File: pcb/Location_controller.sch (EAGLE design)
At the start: 62 parts, among them IC1 LIS302DL

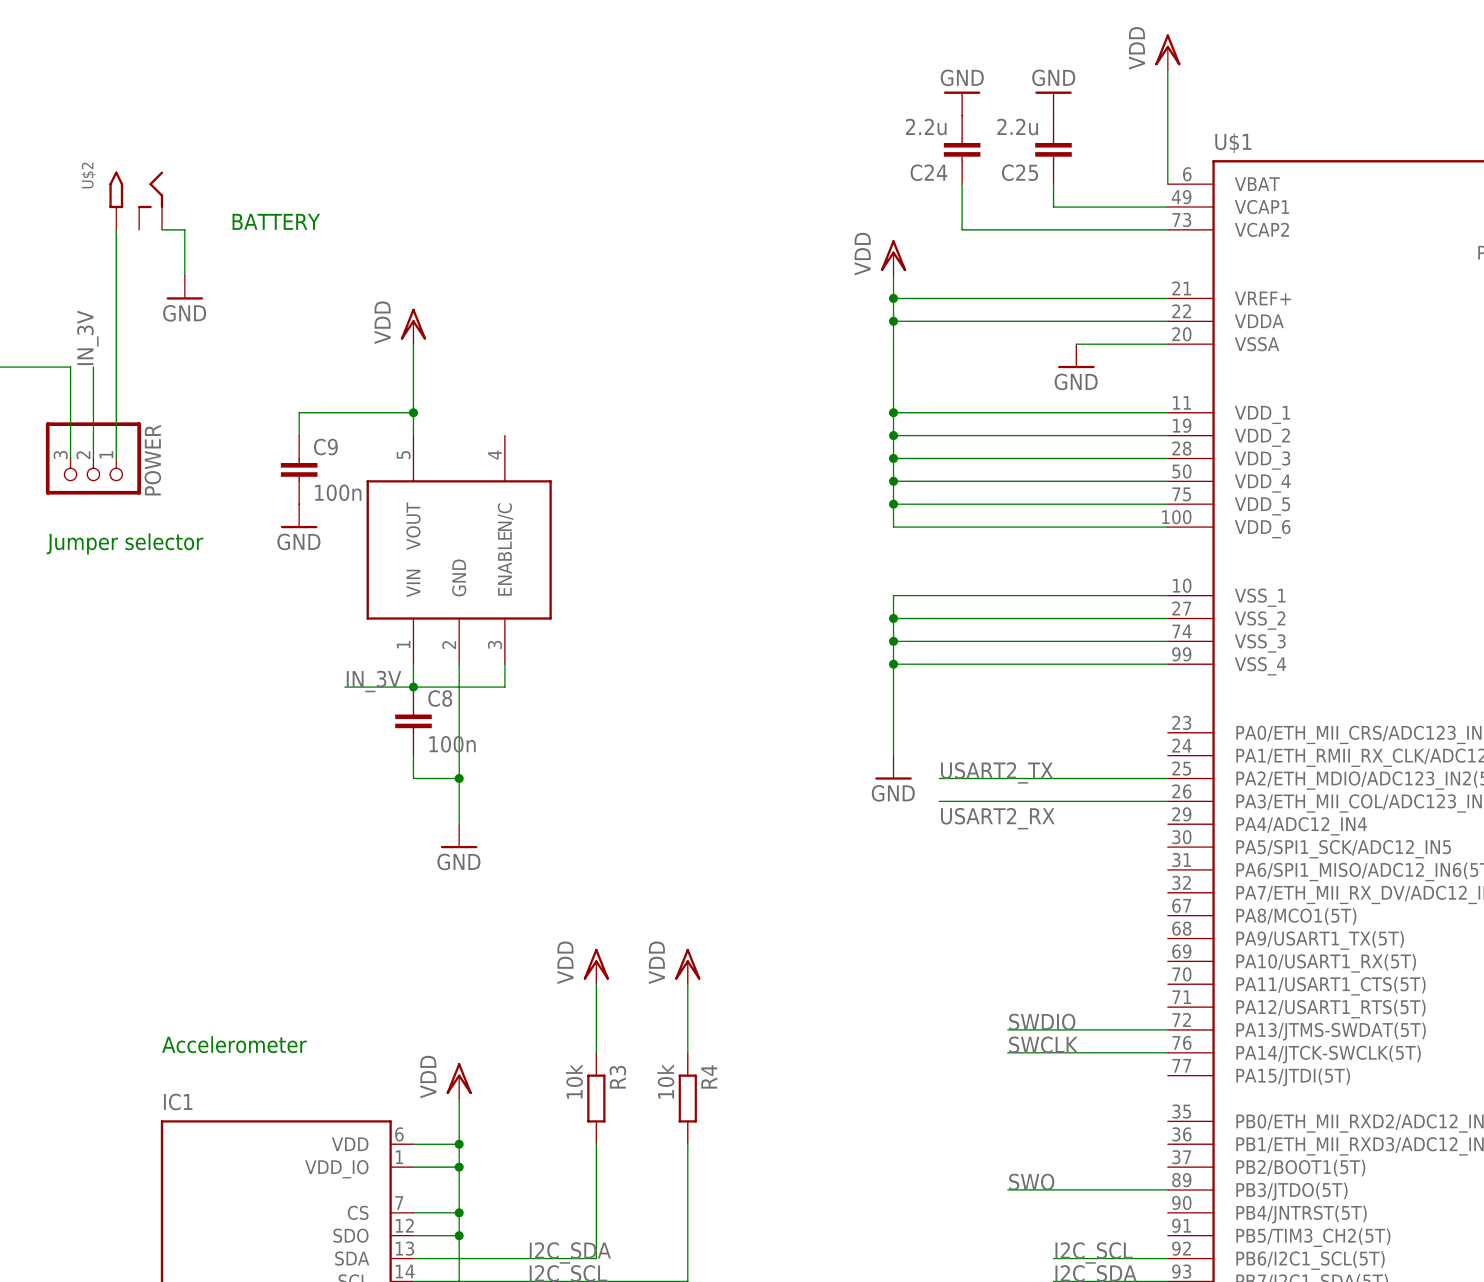
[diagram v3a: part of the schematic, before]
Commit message: Move RCM_POWER pins to correct position
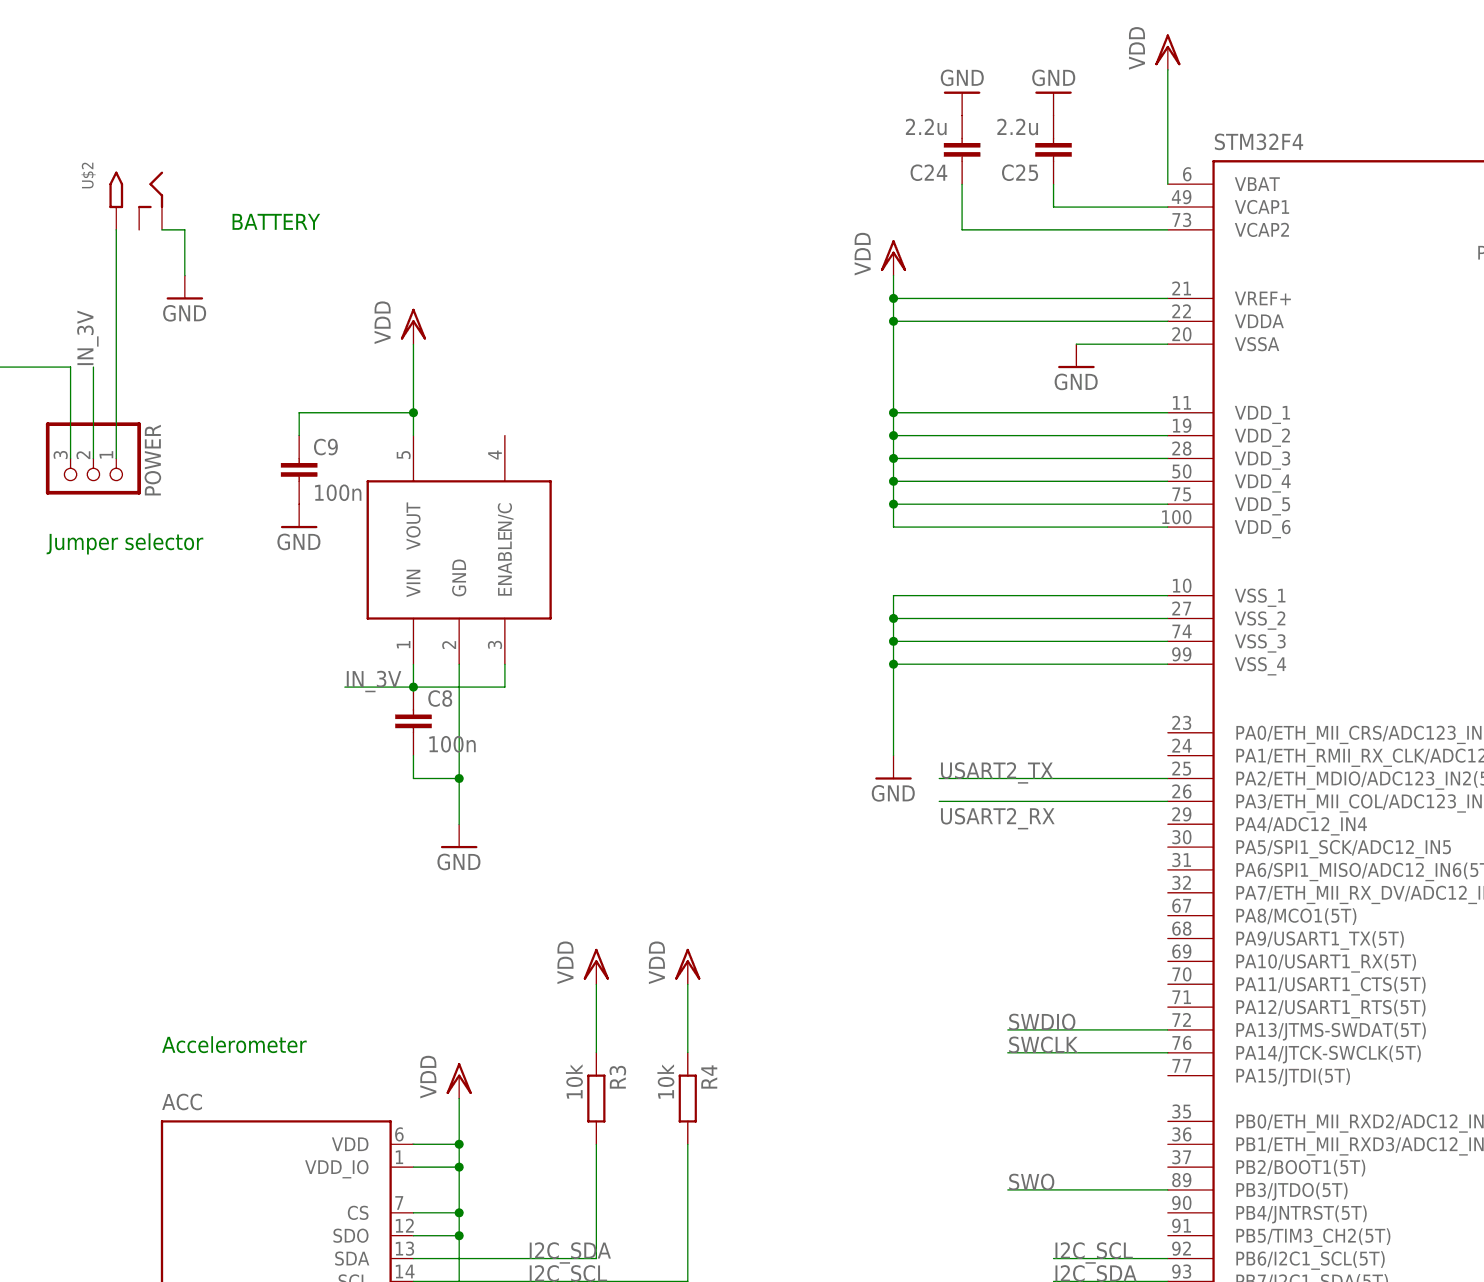
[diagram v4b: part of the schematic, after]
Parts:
- renumbered IC1 to ACC, U$1 to STM32F4

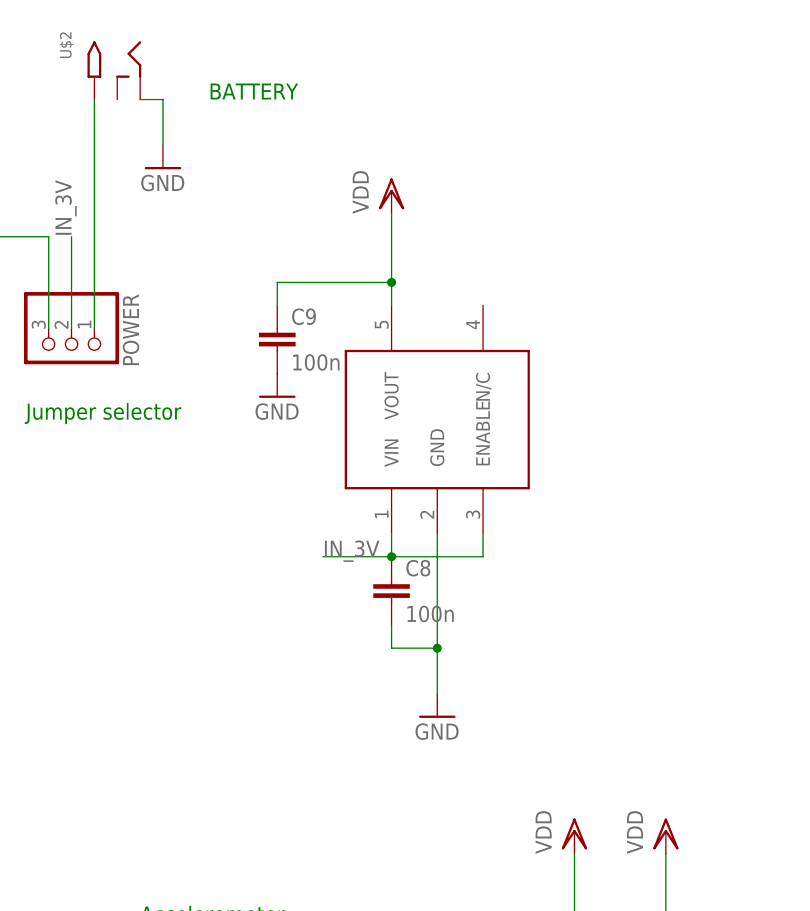
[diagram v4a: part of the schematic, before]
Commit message: Swap voltage regulator for one in stock
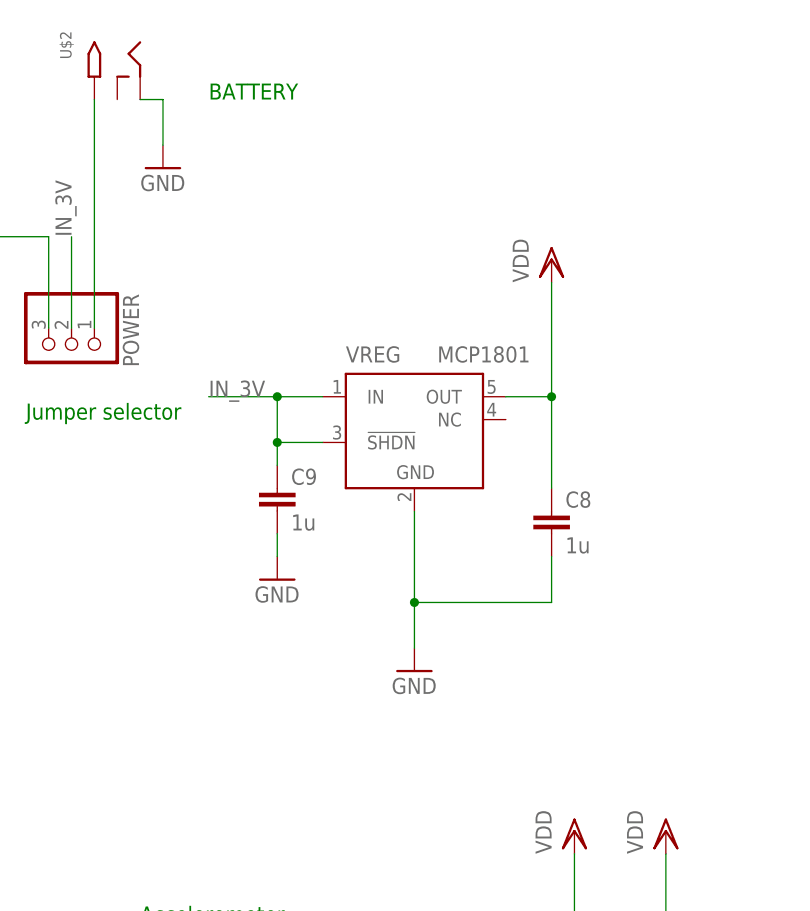
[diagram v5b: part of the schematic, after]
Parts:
- removed REG: NCP551, stm32f4:NCP551
- added VREG: MCP1801, stm32f4:MCP1801
- C8, C9: value 100n -> 1u
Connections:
- net GND: now also VREG.GND; no longer REG.GND
- net IN_3V: now also C9.1, VREG.!SHDN, VREG.IN; no longer C8.1, REG.ENABLE, REG.VIN
- net VDD: now also C8.1, VREG.OUT; no longer C9.1, REG.VOUT
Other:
- moved on the sheet: C8, C9
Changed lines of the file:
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@@
 <part name="GND10" library="supply1" deviceset="GND" device=""/>
 <part name="GND11" library="supply1" deviceset="GND" device=""/>
-<part name="REG" library="stm32f4" deviceset="NCP551" device=""/>
 <part name="GND12" library="supply1" deviceset="GND" device=""/>
 <part name="VDD6" library="supply1" deviceset="VDD" device=""/>
-<part name="C8" library="eagle-ltspice" deviceset="C" device="" value="100n"/>
-<part name="C9" library="eagle-ltspice" deviceset="C" device="" value="100n"/>
+<part name="C8" library="eagle-ltspice" deviceset="C" device="" value="1u"/>
+<part name="C9" library="eagle-ltspice" deviceset="C" device="" value="1u"/>
 <part name="GND13" library="supply1" deviceset="GND" device=""/>
 <part name="GND14" library="supply1" deviceset="GND" device=""/>
@@
 <part name="GND32" library="supply1" deviceset="GND" device=""/>
 <part name="GND33" library="supply1" deviceset="GND" device=""/>
+<part name="VREG" library="stm32f4" deviceset="MCP1801" device=""/>
 </parts>
 <sheets>
@@
 <instance part="GND10" gate="1" x="-38.1" y="-12.7"/>
 <instance part="GND11" gate="1" x="-60.96" y="-12.7"/>
-<instance part="REG" gate="G$1" x="-38.1" y="88.9"/>
-<instance part="GND12" gate="1" x="-38.1" y="58.42"/>
-<instance part="VDD6" gate="G$1" x="-43.18" y="116.84"/>
-<instance part="C8" gate="G$1" x="-43.18" y="73.66"/>
-<instance part="C9" gate="G$1" x="-55.88" y="101.6"/>
-<instance part="GND13" gate="1" x="-55.88" y="93.98"/>
+<instance part="GND12" gate="1" x="-40.64" y="63.5"/>
+<instance part="VDD6" gate="G$1" x="-25.4" y="109.22"/>
+<instance part="C8" gate="G$1" x="-25.4" y="81.28"/>
+<instance part="C9" gate="G$1" x="-55.88" y="83.82"/>
+<instance part="GND13" gate="1" x="-55.88" y="73.66"/>
 <instance part="GND14" gate="1" x="-68.58" y="119.38"/>
 <instance part="GND15" gate="1" x="10.16" y="66.04"/>
@@
 <instance part="GND32" gate="1" x="99.06" y="-88.9"/>
 <instance part="GND33" gate="1" x="106.68" y="-88.9"/>
+<instance part="VREG" gate="G$1" x="-40.64" y="91.44"/>
 </instances>
 <busses>
@@
 </segment>
 <segment>
-<pinref part="REG" gate="G$1" pin="GND"/>
-<pinref part="GND12" gate="1" pin="GND"/>
-<wire x1="-38.1" y1="60.96" x2="-38.1" y2="66.04" width="0.1524" layer="91"/>
-<pinref part="C8" gate="G$1" pin="2"/>
-<wire x1="-38.1" y1="66.04" x2="-38.1" y2="78.74" width="0.1524" layer="91"/>
-<wire x1="-43.18" y1="68.58" x2="-43.18" y2="66.04" width="0.1524" layer="91"/>
-<wire x1="-43.18" y1="66.04" x2="-38.1" y2="66.04" width="0.1524" layer="91"/>
-<junction x="-38.1" y="66.04"/>
-</segment>
-<segment>
 <pinref part="C9" gate="G$1" pin="2"/>
 <pinref part="GND13" gate="1" pin="GND"/>
+<wire x1="-55.88" y1="76.2" x2="-55.88" y2="78.74" width="0.1524" layer="91"/>
 </segment>
 <segment>
@@
 <wire x1="106.68" y1="-73.66" x2="106.68" y2="-86.36" width="0.1524" layer="91"/>
 </segment>
+<segment>
+<pinref part="VREG" gate="G$1" pin="GND"/>
+<pinref part="GND12" gate="1" pin="GND"/>
+<wire x1="-40.64" y1="81.28" x2="-40.64" y2="71.12" width="0.1524" layer="91"/>
+<pinref part="C8" gate="G$1" pin="2"/>
+<wire x1="-40.64" y1="71.12" x2="-40.64" y2="66.04" width="0.1524" layer="91"/>
+<wire x1="-25.4" y1="76.2" x2="-25.4" y2="71.12" width="0.1524" layer="91"/>
+<wire x1="-25.4" y1="71.12" x2="-40.64" y2="71.12" width="0.1524" layer="91"/>
+<junction x="-40.64" y="71.12"/>
+</segment>
 </net>
 <net name="N$1" class="0">
@@
 </segment>
 <segment>
-<pinref part="REG" gate="G$1" pin="VOUT"/>
-<pinref part="C9" gate="G$1" pin="1"/>
-<wire x1="-43.18" y1="106.68" x2="-43.18" y2="104.14" width="0.1524" layer="91"/>
-<wire x1="-55.88" y1="104.14" x2="-55.88" y2="106.68" width="0.1524" layer="91"/>
-<wire x1="-55.88" y1="106.68" x2="-43.18" y2="106.68" width="0.1524" layer="91"/>
-<wire x1="-43.18" y1="114.3" x2="-43.18" y2="106.68" width="0.1524" layer="91"/>
-<junction x="-43.18" y="106.68"/>
-<pinref part="VDD6" gate="G$1" pin="VDD"/>
-</segment>
-<segment>
 <pinref part="R7" gate="G$1" pin="2"/>
 <pinref part="VDD10" gate="G$1" pin="VDD"/>
@@
 <pinref part="VDD2" gate="G$1" pin="VDD"/>
 <wire x1="167.64" y1="-7.62" x2="170.18" y2="-7.62" width="0.1524" layer="91"/>
+</segment>
+<segment>
+<pinref part="VDD6" gate="G$1" pin="VDD"/>
+<wire x1="-25.4" y1="106.68" x2="-25.4" y2="93.98" width="0.1524" layer="91"/>
+<pinref part="VREG" gate="G$1" pin="OUT"/>
+<wire x1="-25.4" y1="93.98" x2="-30.48" y2="93.98" width="0.1524" layer="91"/>
+<pinref part="C8" gate="G$1" pin="1"/>
+<wire x1="-25.4" y1="83.82" x2="-25.4" y2="93.98" width="0.1524" layer="91"/>
+<junction x="-25.4" y="93.98"/>
 </segment>
 </net>
@@
 </segment>
 <segment>
-<pinref part="REG" gate="G$1" pin="VIN"/>
-<pinref part="C8" gate="G$1" pin="1"/>
-<wire x1="-43.18" y1="78.74" x2="-43.18" y2="76.2" width="0.1524" layer="91"/>
-<pinref part="REG" gate="G$1" pin="ENABLE"/>
-<wire x1="-33.02" y1="78.74" x2="-33.02" y2="76.2" width="0.1524" layer="91"/>
-<wire x1="-33.02" y1="76.2" x2="-43.18" y2="76.2" width="0.1524" layer="91"/>
-<junction x="-43.18" y="76.2"/>
-<wire x1="-43.18" y1="76.2" x2="-50.8" y2="76.2" width="0.1524" layer="91"/>
-<label x="-50.8" y="76.2" size="1.778" layer="95"/>
-</segment>
-<segment>
 <pinref part="RCM_POWER" gate="G$1" pin="2"/>
 <wire x1="-124.46" y1="119.38" x2="-124.46" y2="114.3" width="0.1524" layer="91"/>
@@
 <label x="-119.38" y="106.68" size="1.778" layer="95" rot="R90"/>
 </segment>
-</net>
+<segment>
+<pinref part="VREG" gate="G$1" pin="!SHDN"/>
+<pinref part="C9" gate="G$1" pin="1"/>
+<wire x1="-50.8" y1="88.9" x2="-55.88" y2="88.9" width="0.1524" layer="91"/>
+<wire x1="-55.88" y1="88.9" x2="-55.88" y2="86.36" width="0.1524" layer="91"/>
+<wire x1="-55.88" y1="88.9" x2="-55.88" y2="93.98" width="0.1524" layer="91"/>
+<junction x="-55.88" y="88.9"/>
+<pinref part="VREG" gate="G$1" pin="IN"/>
+<wire x1="-55.88" y1="93.98" x2="-50.8" y2="93.98" width="0.1524" layer="91"/>
+<wire x1="-55.88" y1="93.98" x2="-63.5" y2="93.98" width="0.1524" layer="91"/>
+<junction x="-55.88" y="93.98"/>
+<label x="-63.5" y="93.98" size="1.778" layer="95"/>
+</segment>
+</net>

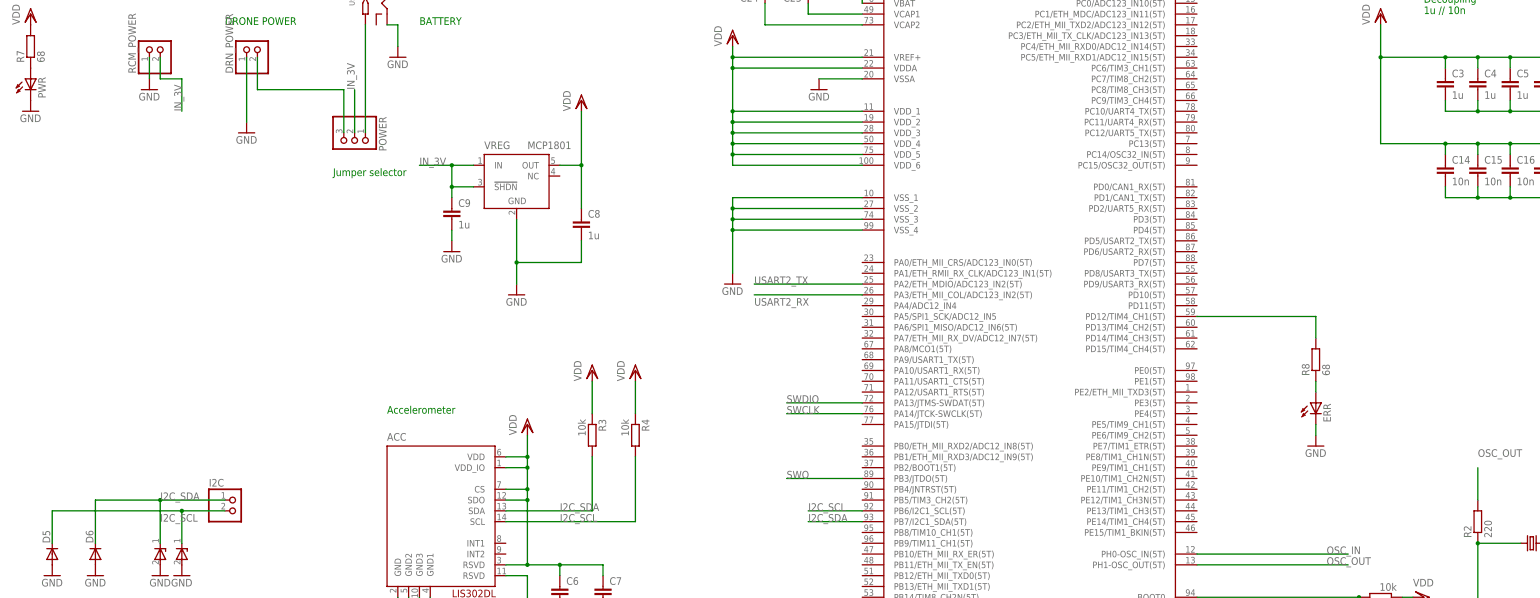
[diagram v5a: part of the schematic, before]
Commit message: Add additional LEDS to board
See pcb/leds.md for pin mapping
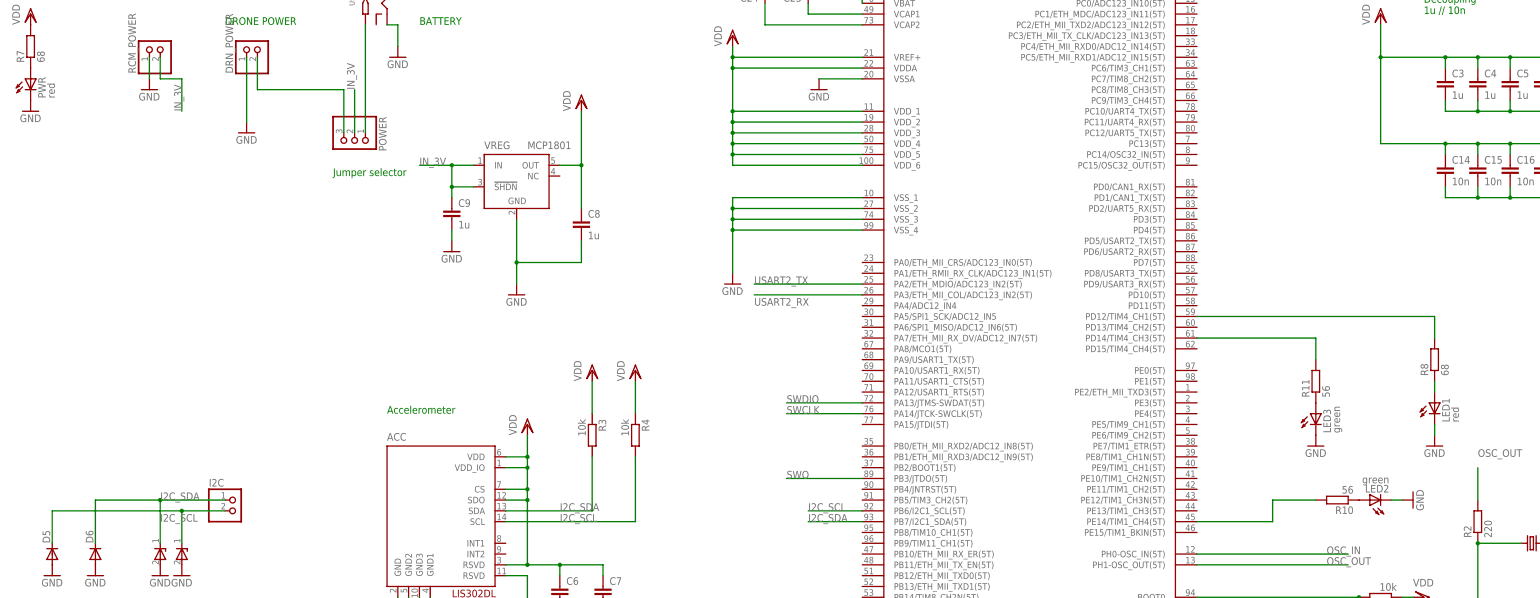
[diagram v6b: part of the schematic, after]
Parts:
- removed ERR: (no value), eagle-ltspice:LED_E
- added LED1: red, led:LEDCHIPLED_0805
- added LED2, LED3: green, led:LEDCHIPLED_0805
- added R10, R11: 56, eagle-ltspice:R
- PWR: value (none) -> red; device eagle-ltspice:LED_E -> led:LEDCHIPLED_0805
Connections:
- new net N$15: LED2.A, R10.1
- new net N$16: R10.2, STM32F4.PE14/TIM1_CH4(5T)
- new net N$17: LED3.A, R11.1
- new net N$19: R11.2, STM32F4.PD14/TIM4_CH3(5T)
- net GND: now also LED1.C, LED2.C, LED3.C; no longer ERR.C
- net N$13: now also LED1.A; no longer ERR.A
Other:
- moved on the sheet: R8
